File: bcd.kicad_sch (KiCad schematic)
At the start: 1 part

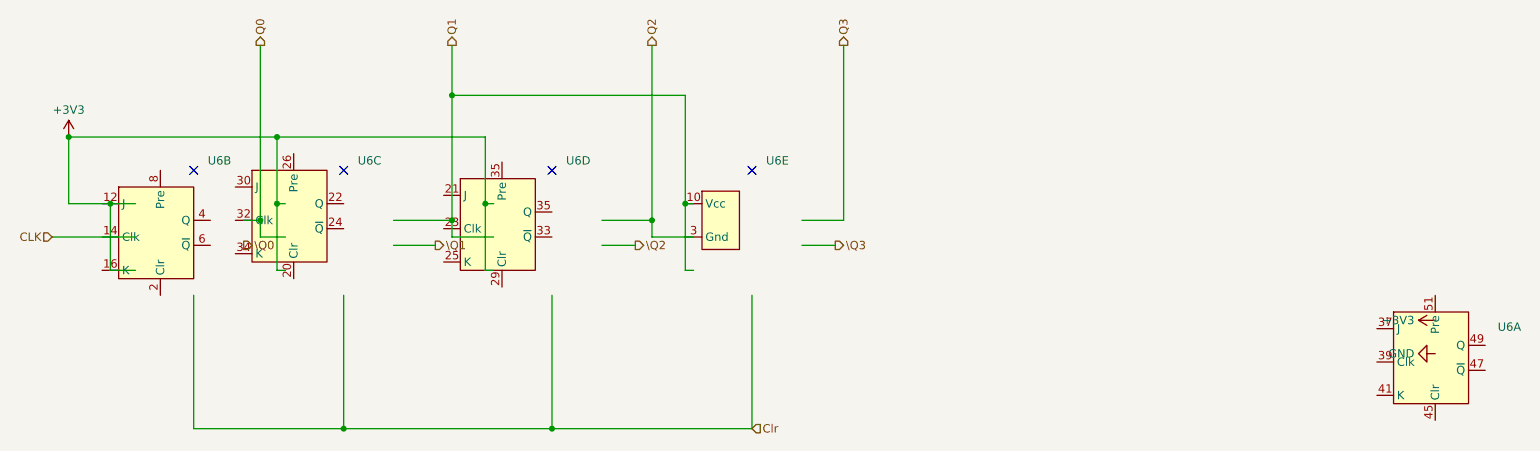
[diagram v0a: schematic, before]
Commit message: changed some components to lcsc parts
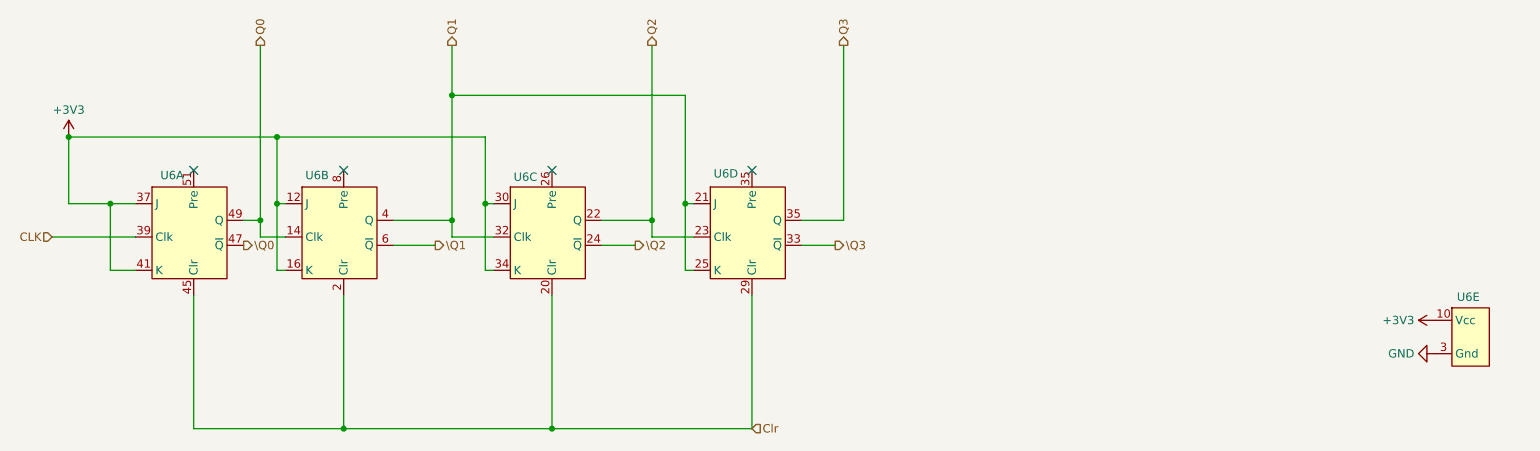
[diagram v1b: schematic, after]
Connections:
- net Gnd is gone; now on net GND: U6.19 (Gnd), U6.27 (Gnd), U6.3 (Gnd), U6.43 (Gnd), U6.9 (Gnd)
- net Vcc is gone; now on net +3V3: U6.10 (Vcc), U6.18 (Vcc), U6.28 (Vcc), U6.36 (Vcc), U6.46 (Vcc)
- net +3V3: now also U6.12 (J), U6.16 (K), U6.30 (J), U6.34 (K), U6.37 (J), U6.41 (K)
- net CLK: now also U6.39 (Clk)
- net Clr: now also U6.2 (Clr), U6.20 (Clr), U6.29 (Clr), U6.45 (Clr)
- net Q0: now also U6.14 (Clk), U6.49 (Q)
- net Q2: now also U6.22 (Q), U6.23 (Clk)
- net Q3: now also U6.35 (Q)
- net \Q0: now also U6.47 (~{Q})
- net \Q1: now also U6.6 (~{Q})
- net \Q2: now also U6.24 (~{Q})
- net \Q3: now also U6.33 (~{Q})
- net Q1: now reaches U6.32 (Clk)
- net Q1: now also U6.21 (J), U6.25 (K), U6.4 (Q)
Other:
- moved on the sheet: U6A, U6B, U6C, U6D, U6E
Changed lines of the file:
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@@
 	(symbol
 		(lib_id "custom:jk-flipflops")
-		(at 85.09 102.87 0)
+		(at 124.46 105.41 0)
 		(unit 3)
 		(exclude_from_sim no)
@@
 		(on_board yes)
 		(dnp no)
-		(fields_autoplaced yes)
 		(property "Reference" "U6"
-			(at 99.9333 102.6625 0)
+			(at 123.698 105.156 0)
 			(effects
 				(font
@@
 		)
 		(property "Value" "~"
-			(at 99.9333 105.0868 0)
-			(effects
-				(font
-					(size 1.27 1.27)
-				)
-				(justify left)
+			(at 139.3033 107.6268 0)
+			(effects
+				(font
+					(size 1.27 1.27)
+				)
+				(justify left)
+				(hide yes)
 			)
 		)
 		(property "Footprint" ""
-			(at 85.09 102.87 0)
+			(at 124.46 105.41 0)
 			(effects
 				(font
@@
 		)
 		(property "Datasheet" ""
-			(at 85.09 102.87 0)
+			(at 124.46 105.41 0)
 			(effects
 				(font
@@
 		)
 		(property "Description" ""
-			(at 85.09 102.87 0)
+			(at 124.46 105.41 0)
 			(effects
 				(font
@@
 		)
 		(property "LCSC Part #" ""
-			(at 85.09 102.87 0)
+			(at 124.46 105.41 0)
 			(effects
 				(font
@@
 		(lib_name "jk-flipflops_2")
 		(lib_id "custom:jk-flipflops")
-		(at 147.32 102.87 0)
+		(at 261.62 120.65 0)
 		(unit 5)
 		(exclude_from_sim no)
@@
 		(on_board yes)
 		(dnp no)
-		(fields_autoplaced yes)
 		(property "Reference" "U6"
-			(at 162.1633 102.6625 0)
+			(at 267.462 123.444 0)
 			(effects
 				(font
@@
 		)
 		(property "Value" "~"
-			(at 162.1633 105.0868 0)
-			(effects
-				(font
-					(size 1.27 1.27)
-				)
-				(justify left)
+			(at 276.4633 122.8668 0)
+			(effects
+				(font
+					(size 1.27 1.27)
+				)
+				(justify left)
+				(hide yes)
 			)
 		)
 		(property "Footprint" ""
-			(at 147.32 102.87 0)
+			(at 261.62 120.65 0)
 			(effects
 				(font
@@
 		)
 		(property "Datasheet" ""
-			(at 147.32 102.87 0)
+			(at 261.62 120.65 0)
 			(effects
 				(font
@@
 		)
 		(property "Description" ""
-			(at 147.32 102.87 0)
+			(at 261.62 120.65 0)
 			(effects
 				(font
@@
 		)
 		(property "LCSC Part #" ""
-			(at 147.32 102.87 0)
+			(at 261.62 120.65 0)
 			(effects
 				(font
@@
 		(lib_name "jk-flipflops_4")
 		(lib_id "custom:jk-flipflops")
-		(at 116.84 104.14 0)
+		(at 154.94 105.41 0)
 		(unit 4)
 		(exclude_from_sim no)
@@
 		(on_board yes)
 		(dnp no)
-		(fields_autoplaced yes)
 		(property "Reference" "U6"
-			(at 131.6833 102.6625 0)
+			(at 154.178 104.648 0)
 			(effects
 				(font
@@
 		)
 		(property "Value" "~"
-			(at 131.6833 105.0868 0)
-			(effects
-				(font
-					(size 1.27 1.27)
-				)
-				(justify left)
+			(at 169.7833 106.3568 0)
+			(effects
+				(font
+					(size 1.27 1.27)
+				)
+				(justify left)
+				(hide yes)
 			)
 		)
 		(property "Footprint" ""
-			(at 116.84 104.14 0)
+			(at 154.94 105.41 0)
 			(effects
 				(font
@@
 		)
 		(property "Datasheet" ""
-			(at 116.84 104.14 0)
+			(at 154.94 105.41 0)
 			(effects
 				(font
@@
 		)
 		(property "Description" ""
-			(at 116.84 104.14 0)
+			(at 154.94 105.41 0)
 			(effects
 				(font
@@
 		)
 		(property "LCSC Part #" ""
-			(at 116.84 104.14 0)
+			(at 154.94 105.41 0)
 			(effects
 				(font
@@
 		(lib_name "jk-flipflops_1")
 		(lib_id "custom:jk-flipflops")
-		(at 259.08 124.46 0)
+		(at 69.85 105.41 0)
 		(unit 1)
 		(exclude_from_sim no)
@@
 		(on_board yes)
 		(dnp no)
-		(fields_autoplaced yes)
 		(property "Reference" "U6"
-			(at 273.685 128.0103 0)
+			(at 69.85 104.902 0)
 			(effects
 				(font
@@
 		)
 		(property "Value" "~"
-			(at 273.685 130.4346 0)
-			(effects
-				(font
-					(size 1.27 1.27)
-				)
-				(justify left)
+			(at 84.455 111.3846 0)
+			(effects
+				(font
+					(size 1.27 1.27)
+				)
+				(justify left)
+				(hide yes)
 			)
 		)
 		(property "Footprint" ""
-			(at 259.08 124.46 0)
+			(at 69.85 105.41 0)
 			(effects
 				(font
@@
 		)
 		(property "Datasheet" ""
-			(at 259.08 124.46 0)
+			(at 69.85 105.41 0)
 			(effects
 				(font
@@
 		)
 		(property "Description" ""
-			(at 259.08 124.46 0)
+			(at 69.85 105.41 0)
 			(effects
 				(font
@@
 		)
 		(property "LCSC Part #" ""
-			(at 259.08 124.46 0)
+			(at 69.85 105.41 0)
 			(effects
 				(font
@@
 		(lib_name "jk-flipflops_3")
 		(lib_id "custom:jk-flipflops")
-		(at 64.77 105.41 0)
+		(at 92.71 105.41 0)
 		(unit 2)
 		(exclude_from_sim no)
@@
 		(on_board yes)
 		(dnp no)
-		(fields_autoplaced yes)
 		(property "Reference" "U6"
-			(at 77.0733 102.6625 0)
+			(at 91.948 104.902 0)
 			(effects
 				(font
@@
 		)
 		(property "Value" "~"
-			(at 77.0733 105.0868 0)
-			(effects
-				(font
-					(size 1.27 1.27)
-				)
-				(justify left)
+			(at 105.0133 105.0868 0)
+			(effects
+				(font
+					(size 1.27 1.27)
+				)
+				(justify left)
+				(hide yes)
 			)
 		)
 		(property "Footprint" ""
-			(at 64.77 105.41 0)
+			(at 92.71 105.41 0)
 			(effects
 				(font
@@
 		)
 		(property "Datasheet" ""
-			(at 64.77 105.41 0)
+			(at 92.71 105.41 0)
 			(effects
 				(font
@@
 		)
 		(property "Description" ""
-			(at 64.77 105.41 0)
+			(at 92.71 105.41 0)
 			(effects
 				(font
@@
 		)
 		(property "LCSC Part #" ""
-			(at 64.77 105.41 0)
-			(effects
-				(font
+			(at 92.71 105.41 0)
+			(effects
+				(font

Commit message: added footprints for modules
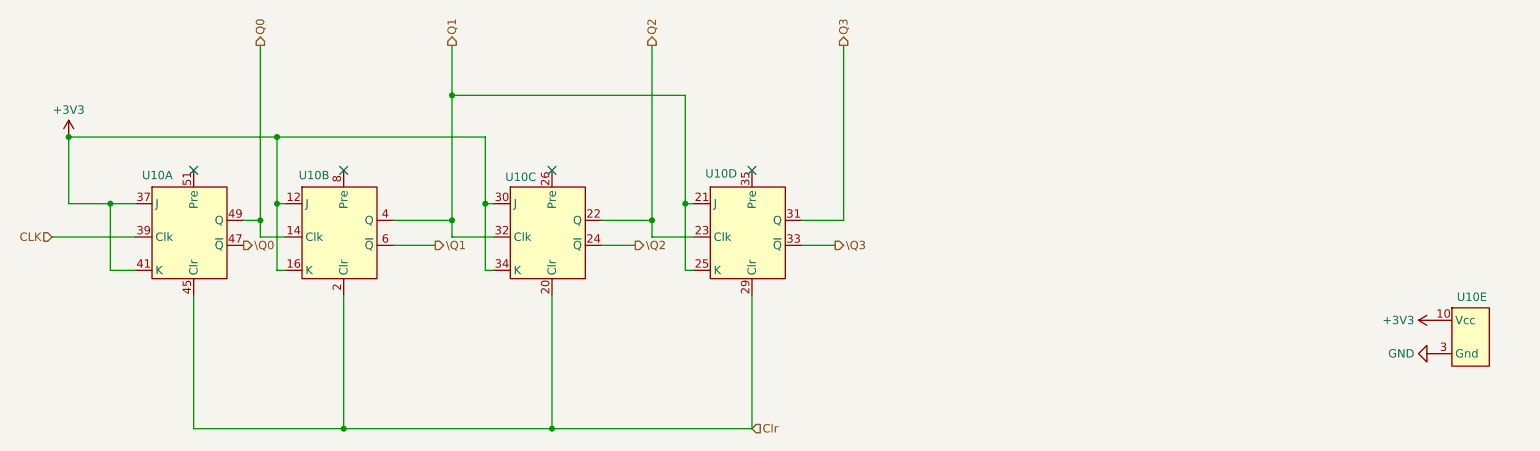
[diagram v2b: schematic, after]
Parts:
- U10: renamed from U6; footprint (none) -> custom:module_flipflop_mpcie
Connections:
- net Q3: now also U10.31 (Q); no longer U10.35 (Q)
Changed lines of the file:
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@@
 		(on_board yes)
 		(dnp no)
-		(property "Reference" "U6"
-			(at 123.698 105.156 0)
+		(property "Reference" "U10"
+			(at 122.428 105.156 0)
 			(effects
 				(font
@@
 			)
 		)
-		(property "Footprint" ""
+		(property "Footprint" "custom:module_flipflop_mpcie"
 			(at 124.46 105.41 0)
 			(effects
@@
 		(pin "10"
 		)
-		(pin "35"
+		(pin "31"
 		)
 		(pin "34"
@@
 			(project "transistor-clock"
 				(path "/ce10d5bc-995e-4952-aa76-0a08f713a0f2/2c36a9e9-de42-4705-9ad4-94f4cc168e2f/213ead95-e2da-4b6f-a756-d929eb6dfb1c"
-					(reference "U8")
+					(reference "U16")
 					(unit 3)
 				)
 				(path "/ce10d5bc-995e-4952-aa76-0a08f713a0f2/2c36a9e9-de42-4705-9ad4-94f4cc168e2f/230aee3b-3cdc-400c-8fed-9199df89dadd"
-					(reference "U6")
+					(reference "U10")
 					(unit 3)
 				)
 				(path "/ce10d5bc-995e-4952-aa76-0a08f713a0f2/2c36a9e9-de42-4705-9ad4-94f4cc168e2f/6fa12e35-b957-4335-be8e-d0857c2dd0bf"
-					(reference "U7")
+					(reference "U13")
 					(unit 3)
 				)
@@
 		(dnp no)
 		(fields_autoplaced yes)
-		(property "Reference" "#PWR018"
+		(property "Reference" "#PWR016"
 			(at 55.88 102.87 0)
 			(effects
@@
 			(project "transistor-clock"
 				(path "/ce10d5bc-995e-4952-aa76-0a08f713a0f2/2c36a9e9-de42-4705-9ad4-94f4cc168e2f/213ead95-e2da-4b6f-a756-d929eb6dfb1c"
-					(reference "#PWR0220")
+					(reference "#PWR035")
 					(unit 1)
 				)
 				(path "/ce10d5bc-995e-4952-aa76-0a08f713a0f2/2c36a9e9-de42-4705-9ad4-94f4cc168e2f/230aee3b-3cdc-400c-8fed-9199df89dadd"
-					(reference "#PWR018")
+					(reference "#PWR016")
 					(unit 1)
 				)
 				(path "/ce10d5bc-995e-4952-aa76-0a08f713a0f2/2c36a9e9-de42-4705-9ad4-94f4cc168e2f/6fa12e35-b957-4335-be8e-d0857c2dd0bf"
-					(reference "#PWR0198")
+					(reference "#PWR020")
 					(unit 1)
 				)
@@
 		(dnp no)
 		(fields_autoplaced yes)
-		(property "Reference" "#PWR014"
+		(property "Reference" "#PWR017"
 			(at 267.97 127 0)
 			(effects
@@
 			(project "transistor-clock"
 				(path "/ce10d5bc-995e-4952-aa76-0a08f713a0f2/2c36a9e9-de42-4705-9ad4-94f4cc168e2f/213ead95-e2da-4b6f-a756-d929eb6dfb1c"
-					(reference "#PWR019")
+					(reference "#PWR036")
 					(unit 1)
 				)
 				(path "/ce10d5bc-995e-4952-aa76-0a08f713a0f2/2c36a9e9-de42-4705-9ad4-94f4cc168e2f/230aee3b-3cdc-400c-8fed-9199df89dadd"
-					(reference "#PWR014")
+					(reference "#PWR017")
 					(unit 1)
 				)
 				(path "/ce10d5bc-995e-4952-aa76-0a08f713a0f2/2c36a9e9-de42-4705-9ad4-94f4cc168e2f/6fa12e35-b957-4335-be8e-d0857c2dd0bf"
-					(reference "#PWR015")
+					(reference "#PWR021")
 					(unit 1)
 				)
@@
 		(dnp no)
 		(fields_autoplaced yes)
-		(property "Reference" "#PWR020"
+		(property "Reference" "#PWR018"
 			(at 257.81 132.08 0)
 			(effects
@@
 			(project "transistor-clock"
 				(path "/ce10d5bc-995e-4952-aa76-0a08f713a0f2/2c36a9e9-de42-4705-9ad4-94f4cc168e2f/213ead95-e2da-4b6f-a756-d929eb6dfb1c"
+					(reference "#PWR037")
+					(unit 1)
+				)
+				(path "/ce10d5bc-995e-4952-aa76-0a08f713a0f2/2c36a9e9-de42-4705-9ad4-94f4cc168e2f/230aee3b-3cdc-400c-8fed-9199df89dadd"
+					(reference "#PWR018")
+					(unit 1)
+				)
+				(path "/ce10d5bc-995e-4952-aa76-0a08f713a0f2/2c36a9e9-de42-4705-9ad4-94f4cc168e2f/6fa12e35-b957-4335-be8e-d0857c2dd0bf"
 					(reference "#PWR022")
-					(unit 1)
-				)
-				(path "/ce10d5bc-995e-4952-aa76-0a08f713a0f2/2c36a9e9-de42-4705-9ad4-94f4cc168e2f/230aee3b-3cdc-400c-8fed-9199df89dadd"
-					(reference "#PWR020")
-					(unit 1)
-				)
-				(path "/ce10d5bc-995e-4952-aa76-0a08f713a0f2/2c36a9e9-de42-4705-9ad4-94f4cc168e2f/6fa12e35-b957-4335-be8e-d0857c2dd0bf"
-					(reference "#PWR021")
 					(unit 1)
 				)
@@
 	)
 	(symbol
-		(lib_name "jk-flipflops_2")
 		(lib_id "custom:jk-flipflops")
 		(at 261.62 120.65 0)
@@
 		(on_board yes)
 		(dnp no)
-		(property "Reference" "U6"
+		(property "Reference" "U10"
 			(at 267.462 123.444 0)
 			(effects
@@
 			)
 		)
-		(property "Footprint" ""
+		(property "Footprint" "custom:module_flipflop_mpcie"
 			(at 261.62 120.65 0)
 			(effects
@@
 		(pin "43"
 		)
-		(pin "35"
+		(pin "31"
 		)
 		(pin "16"
@@
 			(project "transistor-clock"
 				(path "/ce10d5bc-995e-4952-aa76-0a08f713a0f2/2c36a9e9-de42-4705-9ad4-94f4cc168e2f/213ead95-e2da-4b6f-a756-d929eb6dfb1c"
-					(reference "U8")
+					(reference "U16")
 					(unit 5)
 				)
 				(path "/ce10d5bc-995e-4952-aa76-0a08f713a0f2/2c36a9e9-de42-4705-9ad4-94f4cc168e2f/230aee3b-3cdc-400c-8fed-9199df89dadd"
-					(reference "U6")
+					(reference "U10")
 					(unit 5)
 				)
 				(path "/ce10d5bc-995e-4952-aa76-0a08f713a0f2/2c36a9e9-de42-4705-9ad4-94f4cc168e2f/6fa12e35-b957-4335-be8e-d0857c2dd0bf"
-					(reference "U7")
+					(reference "U13")
 					(unit 5)
 				)
@@
 	)
 	(symbol
-		(lib_name "jk-flipflops_4")
 		(lib_id "custom:jk-flipflops")
 		(at 154.94 105.41 0)
@@
 		(on_board yes)
 		(dnp no)
-		(property "Reference" "U6"
-			(at 154.178 104.648 0)
+		(property "Reference" "U10"
+			(at 152.908 104.648 0)
 			(effects
 				(font
@@
 			)
 		)
-		(property "Footprint" ""
+		(property "Footprint" "custom:module_flipflop_mpcie"
 			(at 154.94 105.41 0)
 			(effects
@@
 		(pin "10"
 		)
-		(pin "35"
+		(pin "31"
 		)
 		(pin "34"
@@
 			(project "transistor-clock"
 				(path "/ce10d5bc-995e-4952-aa76-0a08f713a0f2/2c36a9e9-de42-4705-9ad4-94f4cc168e2f/213ead95-e2da-4b6f-a756-d929eb6dfb1c"
-					(reference "U8")
+					(reference "U16")
 					(unit 4)
 				)
 				(path "/ce10d5bc-995e-4952-aa76-0a08f713a0f2/2c36a9e9-de42-4705-9ad4-94f4cc168e2f/230aee3b-3cdc-400c-8fed-9199df89dadd"
-					(reference "U6")
+					(reference "U10")
 					(unit 4)
 				)
 				(path "/ce10d5bc-995e-4952-aa76-0a08f713a0f2/2c36a9e9-de42-4705-9ad4-94f4cc168e2f/6fa12e35-b957-4335-be8e-d0857c2dd0bf"
-					(reference "U7")
+					(reference "U13")
 					(unit 4)
 				)
@@
 	)
 	(symbol
-		(lib_name "jk-flipflops_1")
 		(lib_id "custom:jk-flipflops")
 		(at 69.85 105.41 0)
@@
 		(on_board yes)
 		(dnp no)
-		(property "Reference" "U6"
-			(at 69.85 104.902 0)
+		(property "Reference" "U10"
+			(at 67.056 104.902 0)
 			(effects
 				(font
@@
 			)
 		)
-		(property "Footprint" ""
+		(property "Footprint" "custom:module_flipflop_mpcie"
 			(at 69.85 105.41 0)
 			(effects
@@
 		(pin "10"
 		)
-		(pin "35"
+		(pin "31"
 		)
 		(pin "34"
@@
 			(project "transistor-clock"
 				(path "/ce10d5bc-995e-4952-aa76-0a08f713a0f2/2c36a9e9-de42-4705-9ad4-94f4cc168e2f/213ead95-e2da-4b6f-a756-d929eb6dfb1c"
-					(reference "U8")
+					(reference "U16")
 					(unit 1)
 				)
 				(path "/ce10d5bc-995e-4952-aa76-0a08f713a0f2/2c36a9e9-de42-4705-9ad4-94f4cc168e2f/230aee3b-3cdc-400c-8fed-9199df89dadd"
-					(reference "U6")
+					(reference "U10")
 					(unit 1)
 				)
 				(path "/ce10d5bc-995e-4952-aa76-0a08f713a0f2/2c36a9e9-de42-4705-9ad4-94f4cc168e2f/6fa12e35-b957-4335-be8e-d0857c2dd0bf"
-					(reference "U7")
+					(reference "U13")
 					(unit 1)
 				)
@@
 	)
 	(symbol
-		(lib_name "jk-flipflops_3")
 		(lib_id "custom:jk-flipflops")
 		(at 92.71 105.41 0)
@@
 		(on_board yes)
 		(dnp no)
-		(property "Reference" "U6"
-			(at 91.948 104.902 0)
+		(property "Reference" "U10"
+			(at 90.932 104.902 0)
 			(effects
 				(font
@@
 			)
 		)
-		(property "Footprint" ""
+		(property "Footprint" "custom:module_flipflop_mpcie"
 			(at 92.71 105.41 0)
 			(effects
@@
 		(pin "43"
 		)
-		(pin "35"
+		(pin "31"
 		)
 		(pin "16"
@@
 			(project "transistor-clock"
 				(path "/ce10d5bc-995e-4952-aa76-0a08f713a0f2/2c36a9e9-de42-4705-9ad4-94f4cc168e2f/213ead95-e2da-4b6f-a756-d929eb6dfb1c"
-					(reference "U8")
+					(reference "U16")
 					(unit 2)
 				)
 				(path "/ce10d5bc-995e-4952-aa76-0a08f713a0f2/2c36a9e9-de42-4705-9ad4-94f4cc168e2f/230aee3b-3cdc-400c-8fed-9199df89dadd"
-					(reference "U6")
+					(reference "U10")
 					(unit 2)
 				)
 				(path "/ce10d5bc-995e-4952-aa76-0a08f713a0f2/2c36a9e9-de42-4705-9ad4-94f4cc168e2f/6fa12e35-b957-4335-be8e-d0857c2dd0bf"
-					(reference "U7")
+					(reference "U13")
 					(unit 2)
 				)
